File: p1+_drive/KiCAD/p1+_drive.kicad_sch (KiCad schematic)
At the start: 9 parts, among them J1 SD_Card_Device

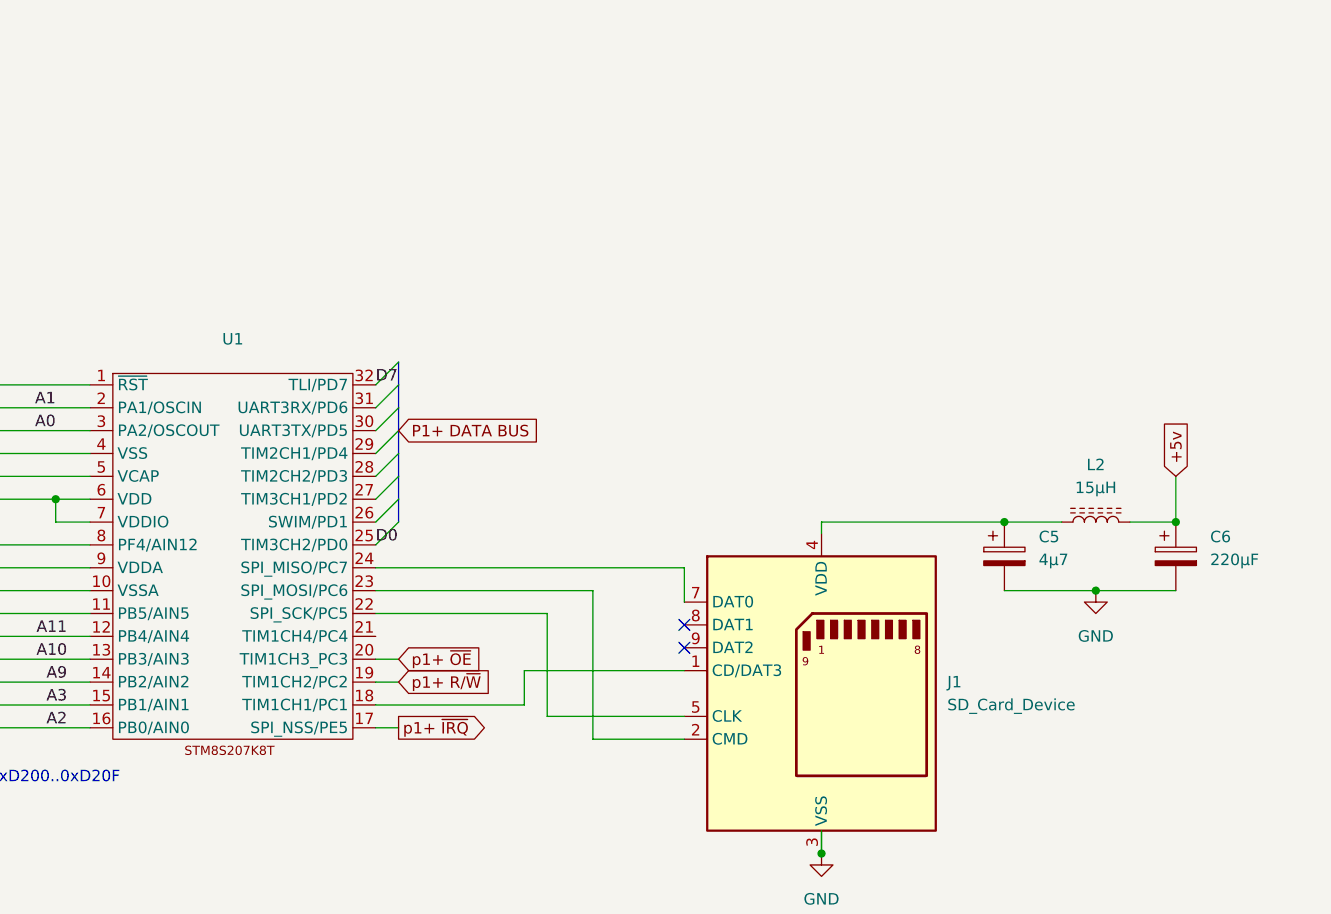
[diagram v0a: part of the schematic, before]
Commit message: Modification à la schématique de p1+_drive
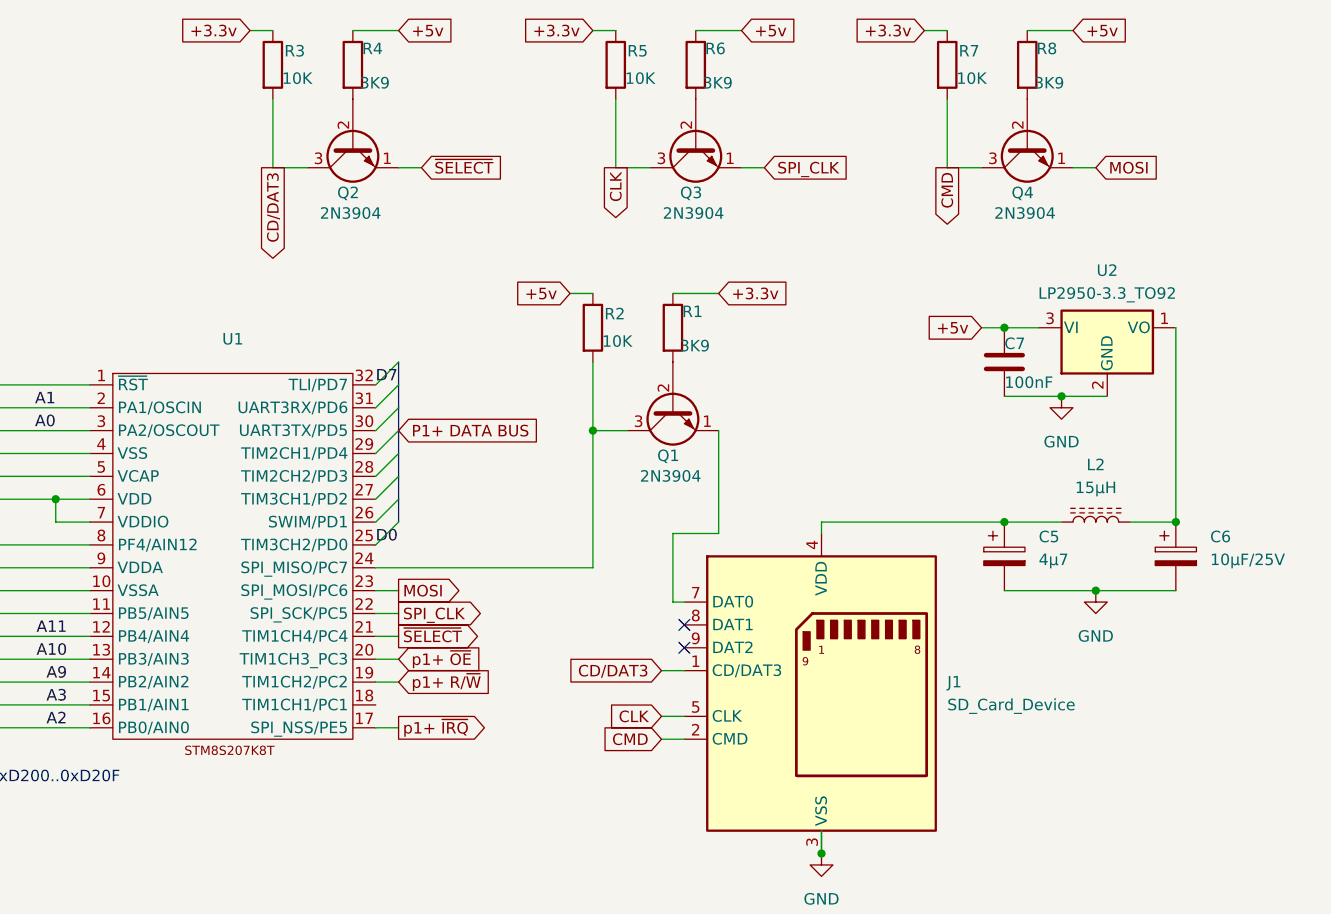
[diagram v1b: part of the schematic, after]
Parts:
- added C7: 100nF, symbol Device:C
- added Q1, Q2, Q3, Q4: 2N3904, Package_TO_SOT_THT:TO-92_Inline, symbol Transistor_BJT:2N3904
- added R1, R4, R6, R8: 3K9, symbol Device:R
- added R2, R3, R5, R7: 10K, symbol Device:R
- added U2: LP2950-3.3_TO92, Package_TO_SOT_THT:TO-92_Inline, symbol Regulator_Linear:LP2950-3.3_TO92
- C6: value 220µF -> 10µF/25V
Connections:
- net +5v: now also C7.1, R2.1, R4.1, R6.1, R8.1, U2.3 (VI); no longer C6.1, L2.2
- net GND: now also C7.2, U2.2 (GND)
- net at U1.18 (TIM1CH1/PC1): no longer J1.1 (CD/DAT3)
- net CMD: now reaches J1.2 (CMD)
- net CMD: now also Q4.3 (C), R7.2; no longer U1.23 (SPI_MOSI/PC6)
- net CLK: now reaches J1.5 (CLK)
- net CLK: now also Q3.3 (C), R5.2; no longer U1.22 (SPI_SCK/PC5)
- net at U1.24 (SPI_MISO/PC7): now also Q1.3 (C), R2.2; no longer J1.7 (DAT0)
- net ~{SELECT}: now reaches U1.21 (TIM1CH4/PC4)
- net ~{SELECT}: now also Q2.1 (E)
- new net: C6.1, L2.2, U2.1 (VO)
- new net: Q3.2 (B), R6.2
- new net: Q2.2 (B), R4.2
- new net: J1.7 (DAT0), Q1.1 (E)
- new net: Q4.2 (B), R8.2
- new net: Q1.2 (B), R1.2
- new net +3.3v: R1.1, R3.1, R5.1, R7.1
- new net CD/DAT3: J1.1 (CD/DAT3), Q2.3 (C), R3.2
- new net MOSI: Q4.1 (E), U1.23 (SPI_MOSI/PC6)
- new net SPI_CLK: Q3.1 (E), U1.22 (SPI_SCK/PC5)

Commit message: test terminal
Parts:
- removed Q1, Q2, Q3, Q4: 2N3904, Package_TO_SOT_THT:TO-92_Inline, symbol Transistor_BJT:2N3904
- removed R1, R4, R6, R8: 3K9, symbol Device:R
- removed R2, R3, R5, R7: 10K, symbol Device:R
- removed U2: LP2950-3.3_TO92, Package_TO_SOT_THT:TO-92_Inline, symbol Regulator_Linear:LP2950-3.3_TO92
- added C8: 100nF, symbol Device:C
- added U2: ~, symbol project_lib:W25Q80DV
- added U3: ~, symbol p1+_drive:LD1117V3.3
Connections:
- net CMD is gone; now on net MOSI: J1.2 (CMD)
- net SPI_CLK is gone; now on net CLK: U1.22 (SPI_SCK/PC5)
- net ~{SELECT} is gone; now on net ~{CS1}: U1.21 (TIM1CH4/PC4)
- net +5v: now also U3.3 (IN); no longer U1.6 (VDD), U1.7 (VDDIO), U1.9 (VDDA)
- net CLK: now also U2.6 (CLK)
- net GND: now also C8.2, U2.4 (GND), U3.2 (GND)
- net MOSI: now also U2.5 (DI)
- net VCAP: no longer U1.8 (PF4/AIN12)
- net p1+ ~{OE}: now also U1.18 (TIM1CH1/PC1); no longer U1.20 (TIM1CH3_PC3)
- net +3.3V: now reaches C6.1, L2.2
- net +3.3V: now also U1.6 (VDD), U1.7 (VDDIO), U1.9 (VDDA), U2.3 (~{WP}), U2.7 (~{HOLD}), U2.8 (VCC), U3.1 (OUT)
- net MISO: now reaches U1.24 (SPI_MISO/PC7)
- net MISO: now also J1.7 (DAT0), U2.2 (DO)
- net CD/DAT3 renamed ~{CS1}
- new net EEPROM: C8.1
- new net ~{SC0}: U1.20 (TIM1CH3_PC3), U2.1 (~{cs})
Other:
- moved on the sheet: C1, C2, C3, C4, C6, C7

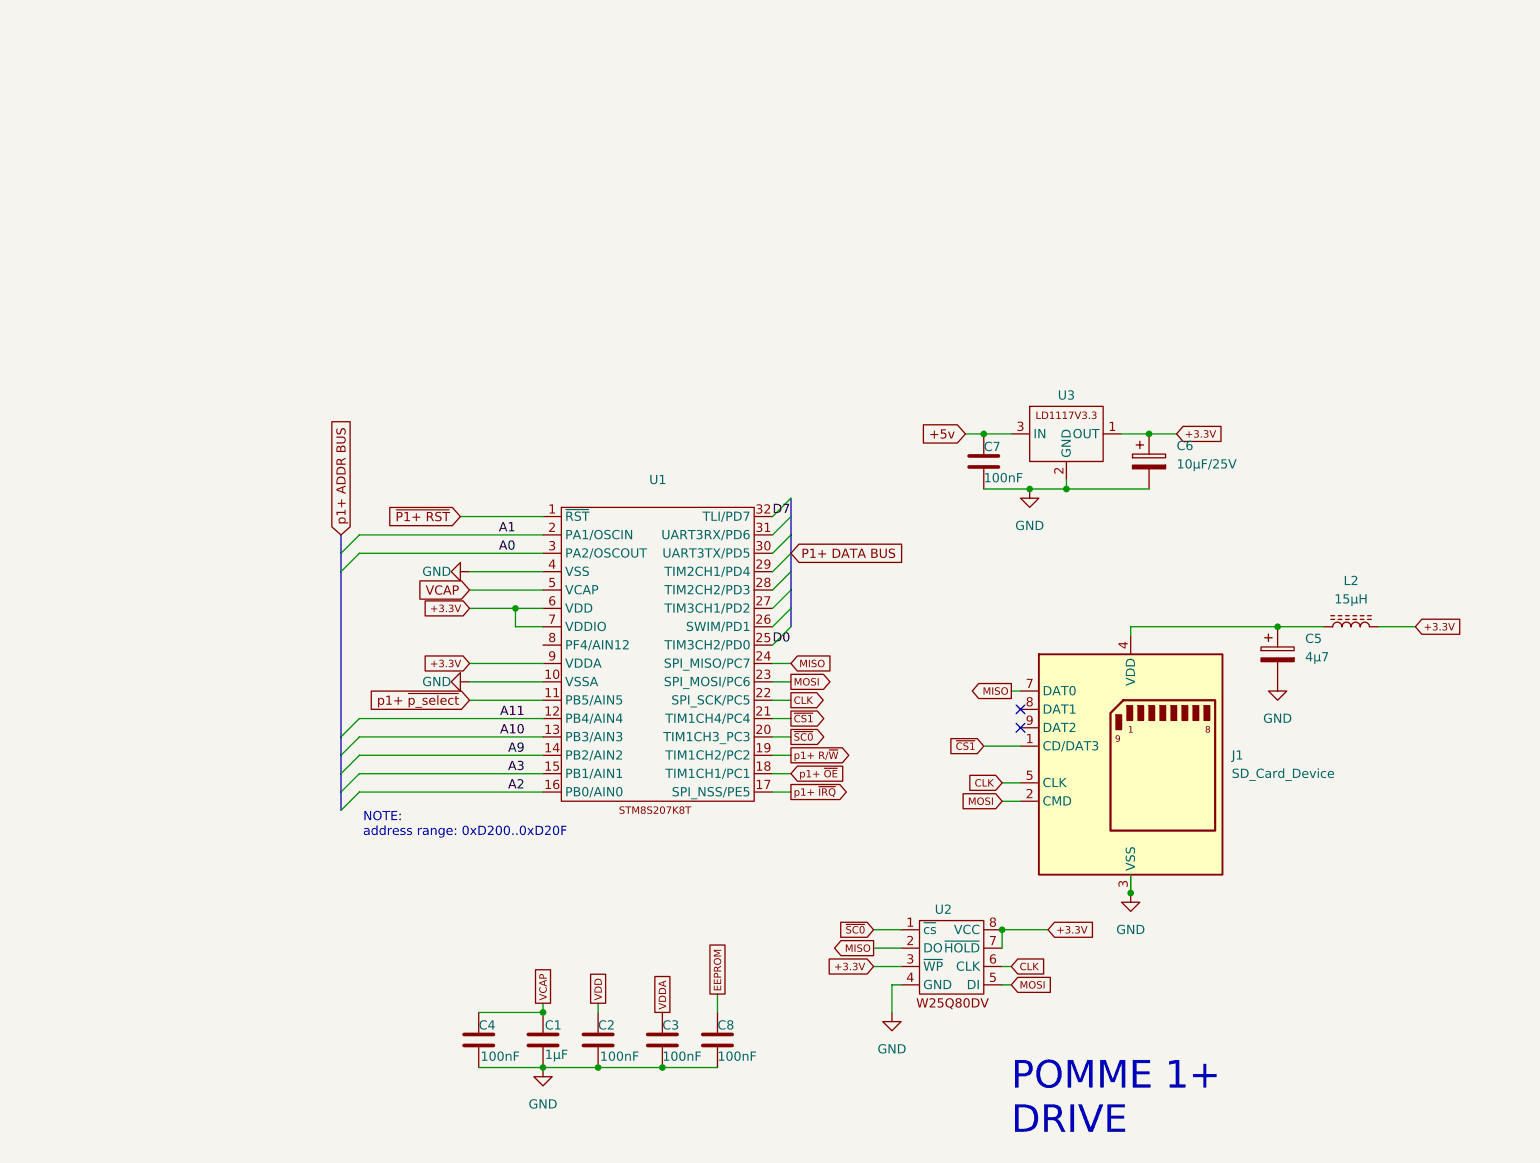
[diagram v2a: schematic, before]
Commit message: spi.asm complété
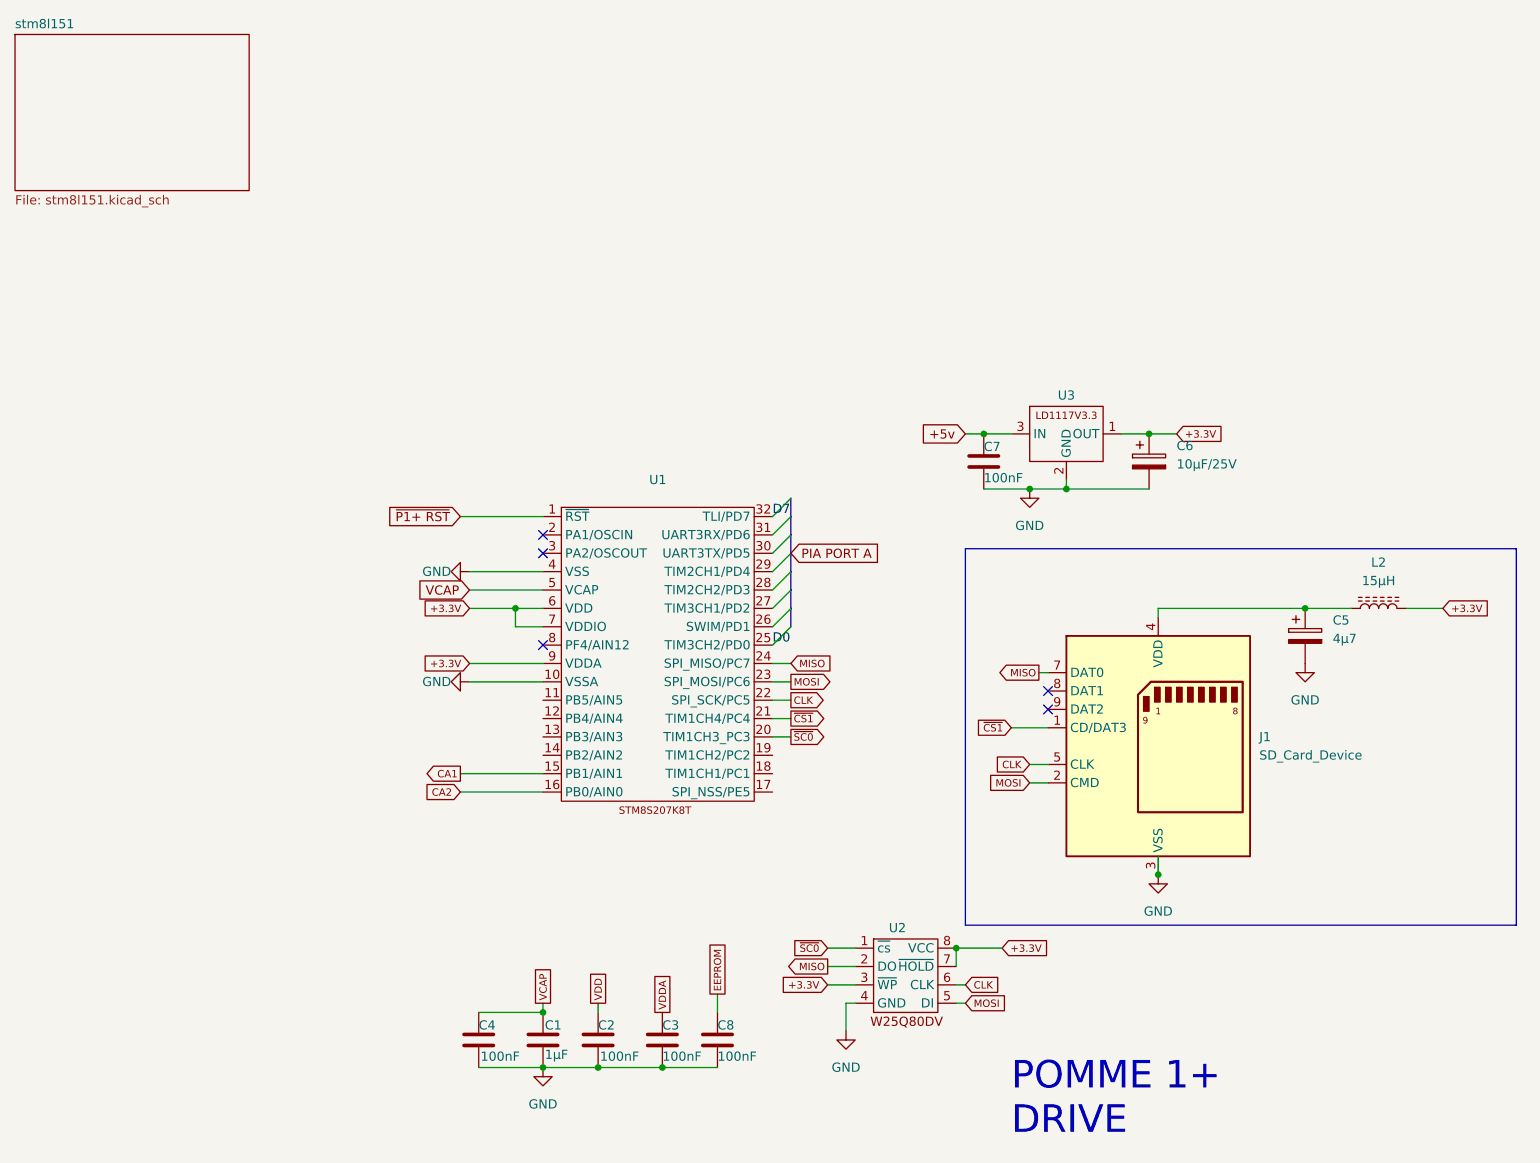
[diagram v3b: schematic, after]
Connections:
- net A0: no longer names the net of U1.3 (PA2/OSCOUT)
- net A1: no longer names the net of U1.2 (PA1/OSCIN)
- net A10: no longer names the net of U1.13 (PB3/AIN3)
- net A11: no longer names the net of U1.12 (PB4/AIN4)
- net A2 renamed CA2
- net A3 renamed CA1
- net A9: no longer names the net of U1.14 (PB2/AIN2)
- net p1+ R/~{W}: no longer names the net of U1.19 (TIM1CH2/PC2)
- net p1+ ~{IRQ}: no longer names the net of U1.17 (SPI_NSS/PE5)
- net p1+ ~{OE}: no longer names the net of U1.18 (TIM1CH1/PC1)
- net p1+ ~{p_select}: no longer names the net of U1.11 (PB5/AIN5)
- no-connect marks 2 -> 5
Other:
- added sheet stm8l151 (stm8l151.kicad_sch)
- note removed: "NOTE: address range: 0xD200..0xD20F"
- moved on the sheet: C5, J1, L2, U2

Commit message: modification schématique p1+_drive
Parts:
- added C11: 100nF, symbol Device:C
- added SW1: interface, symbol Switch:SW_SPST
- added U6: ~, symbol p1+_drive:23LC1024
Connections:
- net +3.3V: now also U6.7 (~{HOLD}/SIO3), U6.8 (VCC)
- net CLK: now also U6.6 (SCK)
- net GND: now also C11.2, SW1.1 (A), U6.3 (SIO2), U6.4 (VSS)
- net MISO: now also U6. (SO/SIO1)
- net MOSI: now also U6.5 (SI/SIO0)
- net ~{CS1}: now also U6.1 (~{CS}); no longer J1.1 (CD/DAT3)
- net at U1.13 (PB3/AIN3): now also SW1.2 (B)
- net ~{SC3}: now reaches U1.18 (TIM1CH1/PC1)
- net ~{SC2}: now reaches U1.19 (TIM1CH2/PC2)
- new net RAM: C11.1
- new net ~{CS2}: J1.1 (CD/DAT3)
- no-connect marks 5 -> 9
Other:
- removed sheet stm8l151
- note added: "128KB RAM"
- note added: "1MB FLASH"
- note added: "SW1"
- note added: "closed"
- note added: "open"
- note added: "optional"
- note added: "parallel"
- note added: "serial"
- moved on the sheet: C1, C2, C3, C4, C8
